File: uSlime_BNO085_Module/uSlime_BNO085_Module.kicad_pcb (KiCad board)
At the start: 2 copper layers, 13 parts, among them J1 Conn_01x05

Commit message: update pcb design
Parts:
- added REF**: MountingHole_2.2mm_M2, MountingHole:MountingHole_2.2mm_M2, F.Cu at (107.2, 107.1)
- added U1: BNO085, BNO_BreakOut:updatedBNO, F.Cu at (99.9, 103.9)
- C1, C2: footprint Capacitor_SMD:C_0402_1005Metric -> Capacitor_SMD:C_0603_1608Metric
- C3, C4: footprint Capacitor_SMD:C_0201_0603Metric -> Capacitor_SMD:C_0603_1608Metric
- JP1: moved to B.Cu
- moved R6 18.7 mm to (106.6, 96.1)
- moved R7 15.1 mm to (102.9, 97.6), turned to 90 degrees
- moved R2 13.2 mm to (106.6, 99.6)
- moved R5 12.7 mm to (106.6, 97.8), turned to 180 degrees
- moved R4 12.4 mm to (101.2, 97.6), turned to -90 degrees
- moved JP1 11.9 mm to (101.1, 97.1)
- moved R3 11.7 mm to (99.4, 97.6), turned to -90 degrees
- moved C1 11.4 mm to (106.6, 101.3), turned to 180 degrees
- moved C2 11.4 mm to (99.9, 107.6), turned to -90 degrees
- moved J1 10.5 mm to (95.9, 97.1)
- moved R1 10.4 mm to (103.4, 107.6), turned to 90 degrees
- moved C3 6.19 mm to (101.7, 107.6), turned to 90 degrees
- moved C4 2.22 mm to (106.6, 103.1), turned to 180 degrees
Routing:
- net +3.3V: track 0.00 -> 47.9 mm, vias 0 -> 1
- net GND: track 0.00 -> 25.4 mm, vias 0 -> 2
- net BNO_INT2: track 0.00 -> 14.0 mm, vias 0 -> 1
- net BNO_SDA: track 0.00 -> 10.9 mm, vias 0 -> 1
- net BNO_SCL: track 0.00 -> 7.69 mm, vias 0 -> 1
- net Net-(U1-ENV_SCL): track 0.00 -> 5.24 mm
- net Net-(U1-NRST): track 0.00 -> 4.18 mm
- net Net-(JP1-C): track 0.00 -> 3.24 mm, vias 0 -> 1
- net Net-(U1-BOOTN): track 0.00 -> 2.91 mm
- net Net-(U1-CAP): track 0.00 -> 2.78 mm
- net Net-(U1-ENV_SDA): track 0.00 -> 1.99 mm
- added copper zone on B.Cu, net GND
- added copper zone on F.Cu, net GND
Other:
- board outline added: 16.8 x 16.2 mm
- board text added: "4A"
- board text added: "4B"

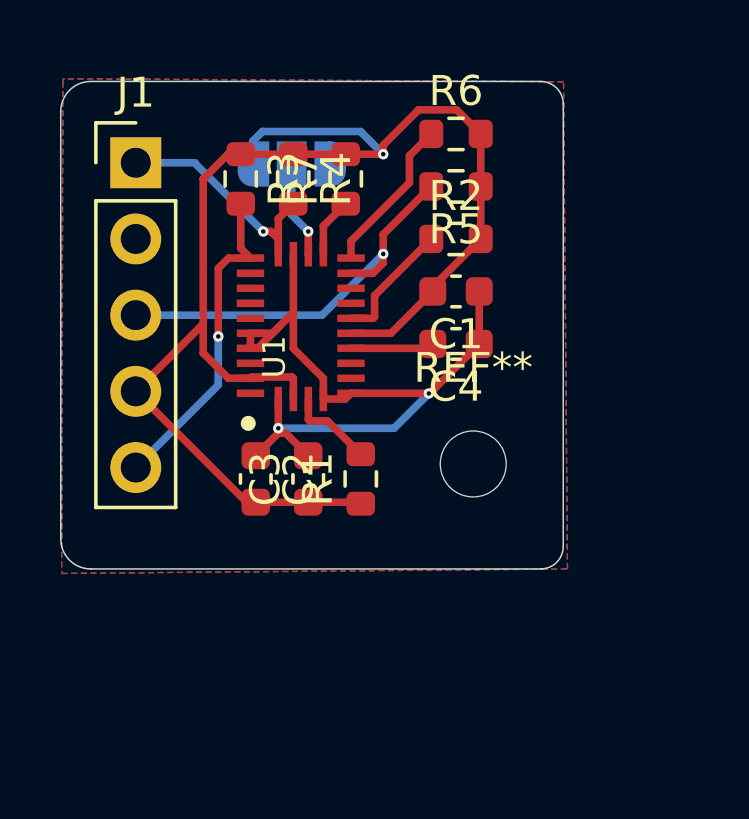
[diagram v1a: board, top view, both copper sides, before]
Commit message: Update uSlime_BNO085_Module.kicad_pcb
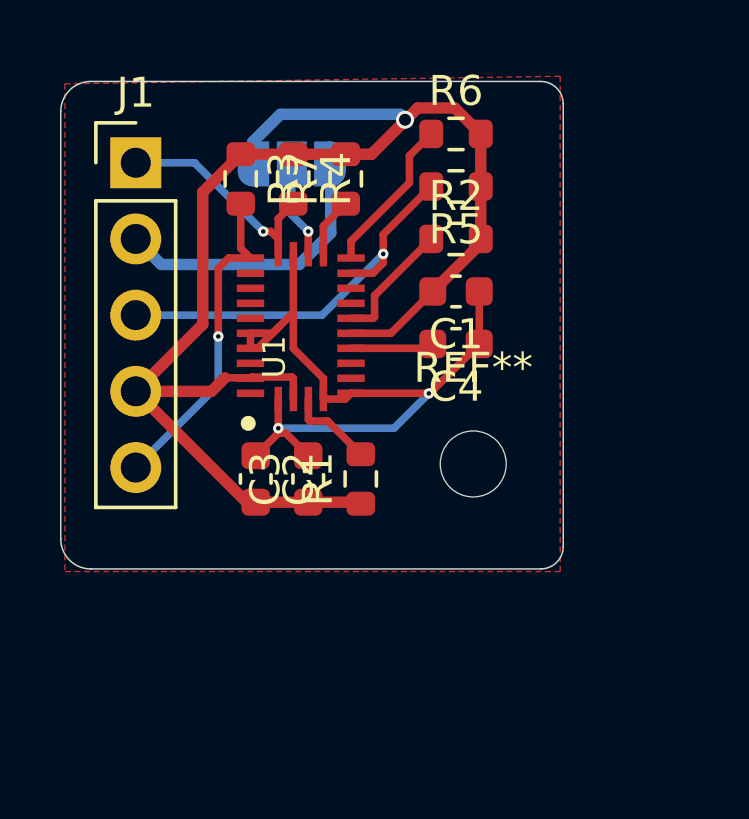
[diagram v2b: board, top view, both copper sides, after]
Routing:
- net GND: track 25.4 -> 35.0 mm
- net +3.3V: track 47.9 -> 49.5 mm
- removed copper zone on B.Cu, net GND

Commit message: update datasheets
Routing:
- added copper zone on B.Cu, net GND
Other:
- board size 16.8 x 16.2 mm -> 16.8 x 15.5 mm
